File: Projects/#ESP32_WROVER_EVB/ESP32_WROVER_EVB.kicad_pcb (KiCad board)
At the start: 2 copper layers, 38 parts, among them J1 CQ-USB-C16PSMT01, Q1 Q_NPN_BEC, Q2 Q_NPN_BEC, SW1 SW_Push, SW2 SW_Push, U1 C3_13U, U2 CP2102N-QFN28, U3 MP214x

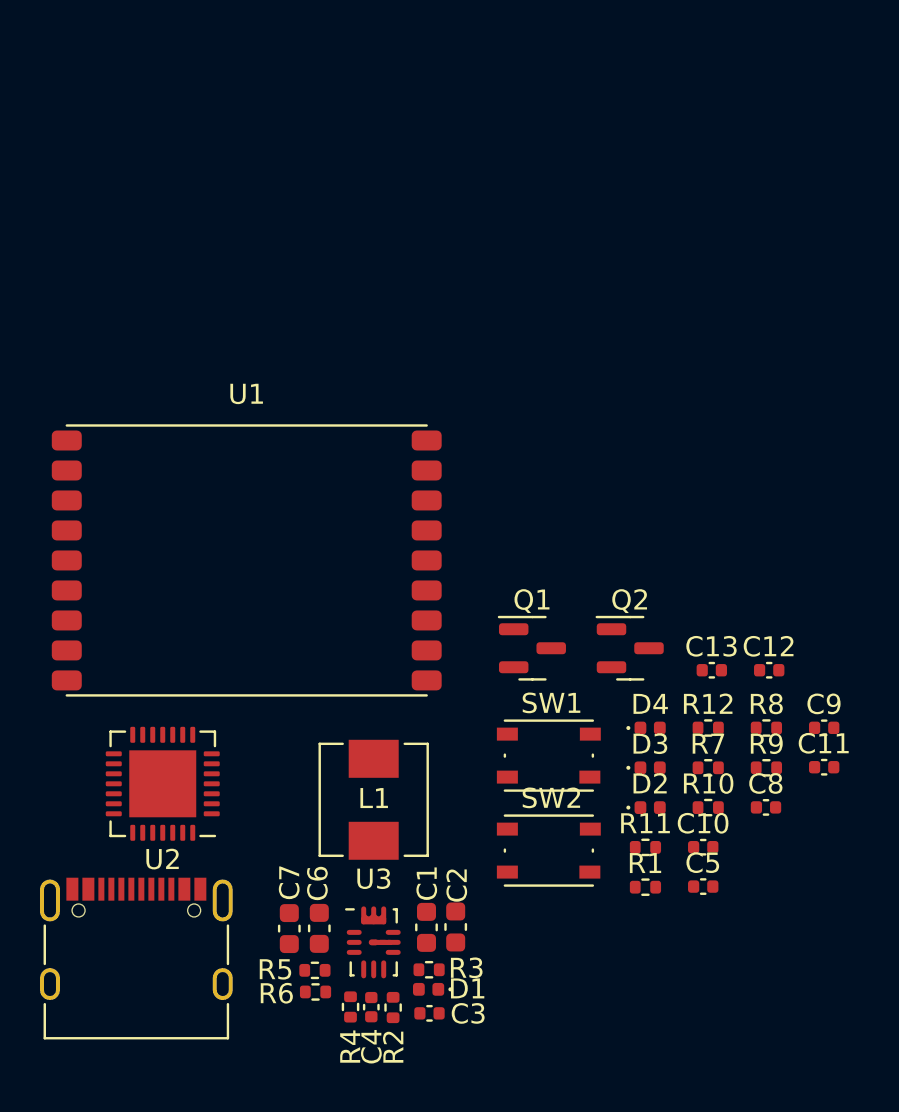
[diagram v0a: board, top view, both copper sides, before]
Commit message: update ESP module
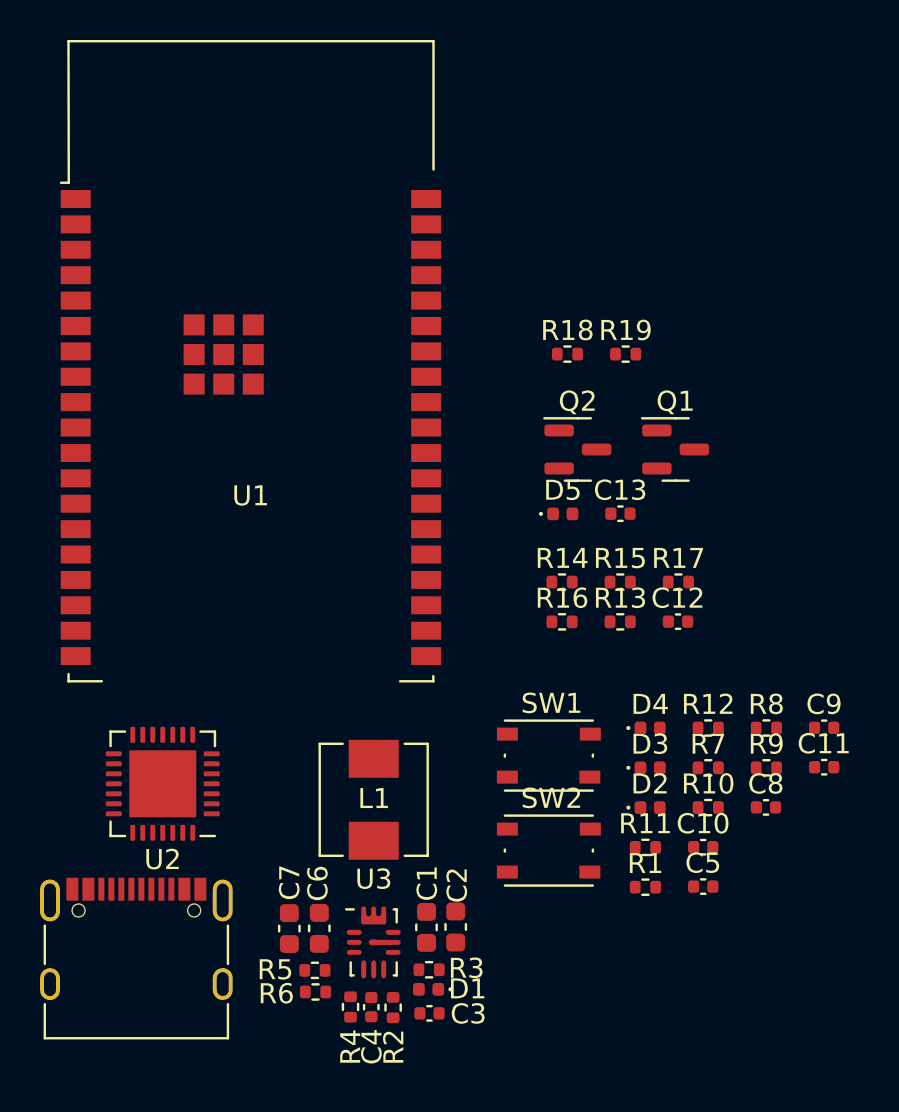
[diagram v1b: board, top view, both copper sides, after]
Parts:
- added D5: LED, LED_SMD:LED_0402_1005Metric, F.Cu at (146.4, 83.5)
- added R13: 10K, Resistor_SMD:R_0402_1005Metric, F.Cu at (149.3, 88.9)
- added R14: 1K, Resistor_SMD:R_0402_1005Metric, F.Cu at (146.4, 86.9)
- added R15: 4K7, Resistor_SMD:R_0402_1005Metric, F.Cu at (149.3, 86.9)
- added R16: 4K7, Resistor_SMD:R_0402_1005Metric, F.Cu at (146.4, 88.9)
- added R17: 4K7, Resistor_SMD:R_0402_1005Metric, F.Cu at (152.2, 86.9)
- added R18: 470R, Resistor_SMD:R_0402_1005Metric, F.Cu at (146.7, 75.5)
- added R19: 470R, Resistor_SMD:R_0402_1005Metric, F.Cu at (149.6, 75.5)
- C13: value 1uF -> 0.1uF
- C8: value 0.1uF -> 1uF
- U1: value C3_13U -> ESP32_WROVER; footprint lib:ESP32_C3_13U -> lib:ESP32-WROVER
- moved Q1 12.3 mm to (152.1, 80.3)
- moved Q2 10.3 mm to (147.2, 80.3)
- moved C13 9.07 mm to (149.3, 83.5)
- moved U1 6.52 mm to (130.8, 79.3)
- moved C12 5.17 mm to (152.2, 88.9)
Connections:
- net ESP_IO0 renamed ESP_SD3
- net ESP_IO1 renamed ESP_SD2
- net ESP_IO10 renamed ESP_IO25
- net ESP_IO6 renamed ESP_S_N
- net ESP_IO7 renamed ESP_IO34
- C12 pad 1: GND -> ESP_EN
- C12 pad 2: ESP_EN -> Net-(C12-Pad2)
- C13 pad 1: GND -> Net-(C13-Pad1)
- C13 pad 2: ESP_BOOT -> GND
- C5 pad 1: GND -> ESP_BOOT
- C5 pad 2: 5V -> Net-(C5-Pad2)
- C9 pad 1: Net-(C9-Pad1) -> GND
- C9 pad 2: GND -> 5V
- U1 pad 1: 3.3V -> GND
- U1 pad 11: ESP_RX -> ESP_IO26
- U1 pad 12: ESP_TX -> ESP_IO27
- U1 pad 13: ESP_IO18 -> JTAG_TMS
- U1 pad 14: ESP_IO19 -> JTAG_TDI
- U1 pad 15: ESP_IO3 -> GND
- U1 pad 16: ESP_IO2 -> JTAG_TCK
- U1 pad 2: ESP_EN -> 3.3V
- U1 pad 3: ESP_IO4 -> ESP_EN
- U1 pad 4: ESP_IO5 -> ESP_S_P
- U1 pad 7: unconnected-(U1-Pad7) -> ESP_IO35
- U1 pad 8: ESP_BOOT -> ESP_IO32
- U1 pad 9: GND -> ESP_IO33
- U2 pad 6: Net-(C9-Pad1) -> Net-(C13-Pad1)
